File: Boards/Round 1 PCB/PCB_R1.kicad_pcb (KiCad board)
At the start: 2 copper layers, 98.4 x 93.1 mm, 67 parts, among them J1 Screw_Terminal_01x12, J10 Screw_Terminal_01x03, J11 Screw_Terminal_01x12, J12 Screw_Terminal_01x03, J13 Screw_Terminal_01x03, J14 Screw_Terminal_01x03, J15 Screw_Terminal_01x03, J16 Screw_Terminal_01x03, J17 Screw_Terminal_01x03, J18 Screw_Terminal_01x03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

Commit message: PCB Design contraints
Updated and tested width and clearene constraints and everything was ok, one unconnected thing. Footprints not updated
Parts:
- C14, C15: value C -> 180uF
- C17: value C -> 2.2uF
- C8, C9: value C -> 20nF
- D3: value SP0503BAHT -> SP0503BAHTG
- L1: value L -> 60uH
- L2: value L -> 2.2uH
- R1, R3: value R_UVLO -> 40K
- R2: value R_UVLO_2 -> 20k
- R4: value R_UVLO_2 -> 20K
- R5: value R_FB_1 -> 2.8K
- R6, R8: value R_FB_2 -> 1K
- R7: value R_FB_1 -> 1.5K
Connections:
- net /V_in renamed +7.5V
- U1 pad 13: /3.3V_OUT -> +3.3V

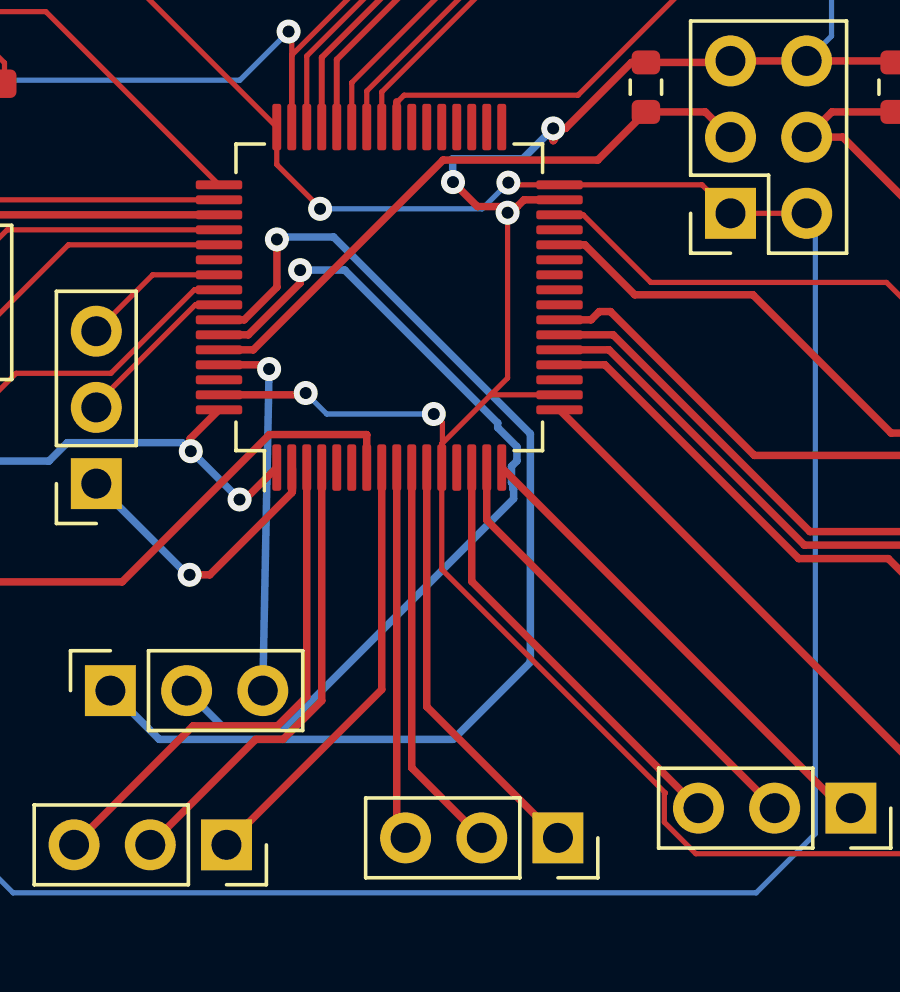
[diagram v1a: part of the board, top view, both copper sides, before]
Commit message: fixed PCB contraints and re-routed something that broke
yea, that
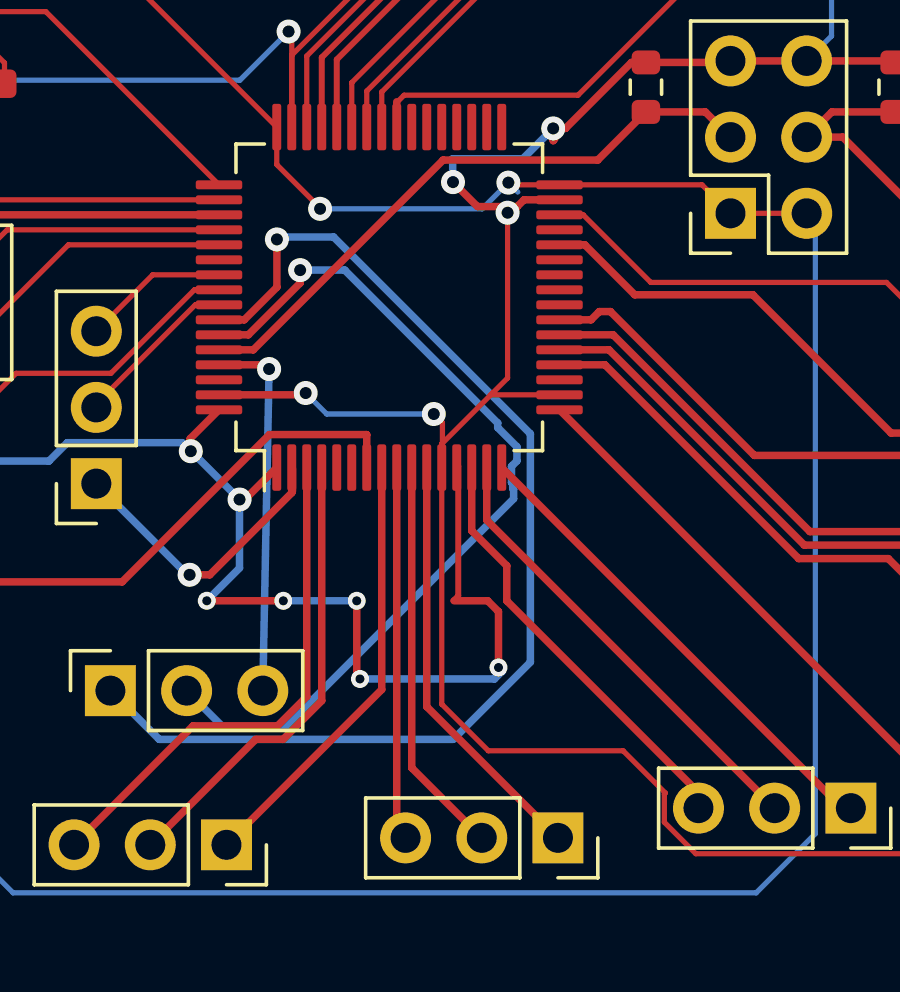
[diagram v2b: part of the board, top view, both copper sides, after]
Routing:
- net +3.3V: track 269.5 -> 294.6 mm, vias 8 -> 13
- net GND: track 612.0 -> 614.6 mm

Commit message: R1 - no builder errors
woot woot
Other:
- board size 98.4 x 93.1 mm -> 97 x 89.5 mm
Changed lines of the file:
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@@
     )
   )
-  (gr_rect (start 50.292 30.099) (end 148.717 123.19)
+  (gr_rect (start 52 31) (end 149 120.5)
     (stroke (width 0.1) (type default)) (fill none) (layer "Edge.Cuts"))
   (dimension (type aligned) (layer "F.Cu")
-    (pts (xy 50.165 30.48) (xy 148.59 30.099))
+    (pts (xy 50.165 30.48) (xy 150 30))
     (height -6.240529)
-    (gr_text "98.4257 mm" (at 99.346375 22.249031 0.2217890065) (layer "F.Cu")
+    (gr_text "99.8362 mm" (at 100.043842 22.199564 0.2754721516) (layer "F.Cu")
       (effects (font (size 1.5 1.5) (thickness 0.3)))
     )
@@
   )
   (dimension (type aligned) (layer "F.Cu")
-    (pts (xy 150.622 30.353) (xy 150.749 123.317))
-    (height -15.259748)
-    (gr_text "92.9641 mm" (at 167.745232 76.811694 270.0782729) (layer "F.Cu")
+    (pts (xy 150.5 28) (xy 150.749 123.317))
+    (height -15.751651)
+    (gr_text "95.3173 mm" (at 168.176091 75.61265 270.1496755) (layer "F.Cu")
       (effects (font (size 1.5 1.5) (thickness 0.3)))
     )
@@
     (polygon
       (pts
-        (xy 50.165 30.48)
-        (xy 148.59 30.099)
-        (xy 148.717 123.063)
-        (xy 50.164999 123.444)
+        (xy 50.665 28.48)
+        (xy 150.5 28)
+        (xy 150 123.063)
+        (xy 50.164999 122.5)
         (xy 50.292 36.703)
       )
@@
     (polygon
       (pts
-        (xy 50.165 30.48)
-        (xy 148.59 30.226)
-        (xy 148.717 122.809)
-        (xy 50.419 123.19)
-        (xy 50.419 29.972)
+        (xy 50.665 28.5)
+        (xy 149.5 28.5)
+        (xy 150 122.809)
+        (xy 50.419 122.5)
+        (xy 50.5 29.972)
       )
     )

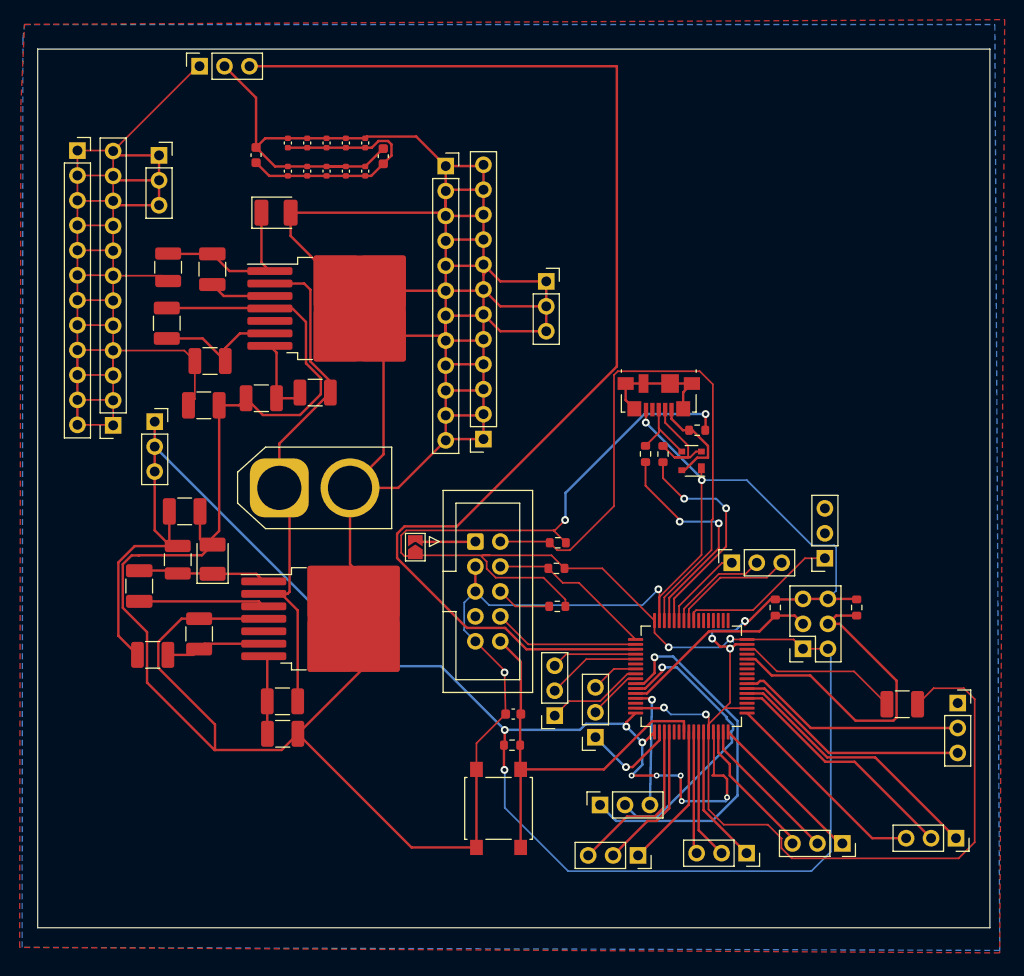
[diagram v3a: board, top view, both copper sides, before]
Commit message: r1 SMD footprint updates
changed component footprints on the board and schematic to use free smd components
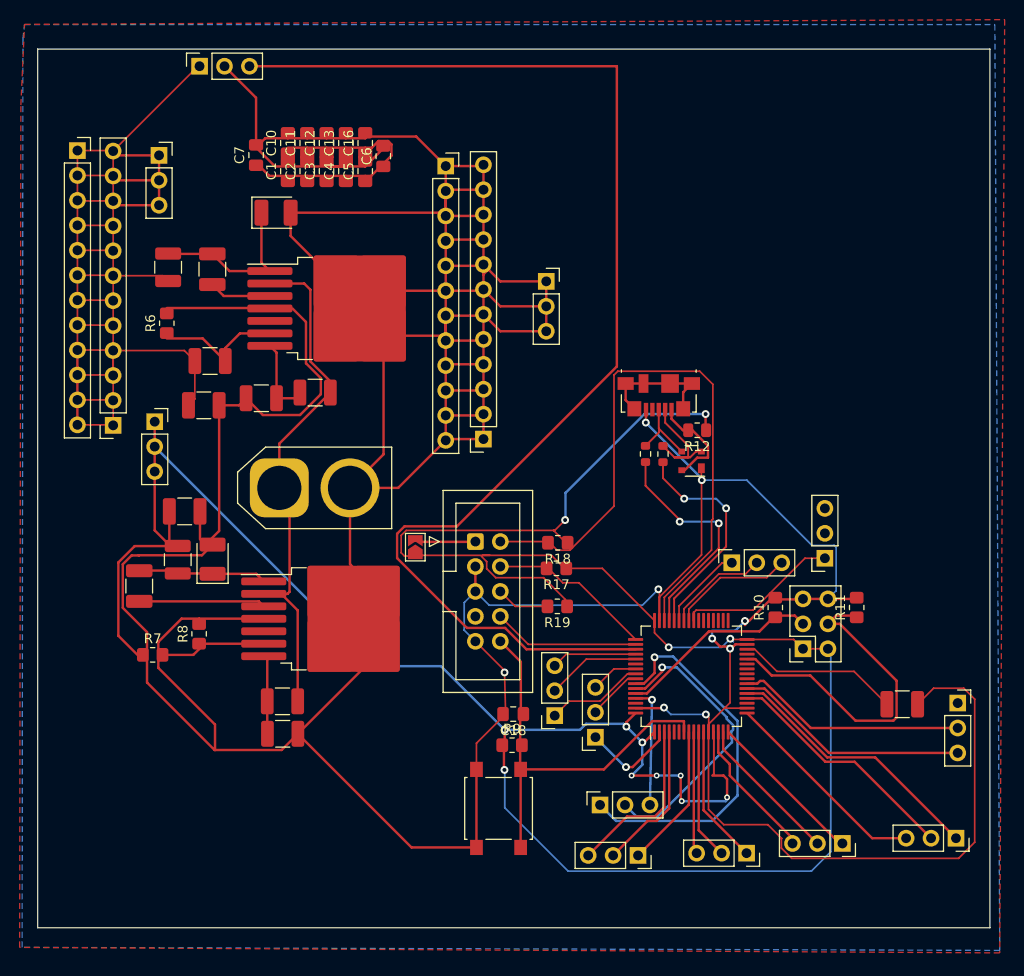
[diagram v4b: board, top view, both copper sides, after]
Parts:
- C1, C10, C11, C12, C13, C16, C2, C3, C4, C5: footprint Capacitor_SMD:C_0402_1005Metric -> Capacitor_SMD:C_0805_2012Metric_Pad1.18x1.45mm_HandSolder
- C18, C6, C7: footprint Capacitor_SMD:C_0603_1608Metric -> Capacitor_SMD:C_0805_2012Metric_Pad1.18x1.45mm_HandSolder
- R10, R11, R17, R18, R19, R9: footprint Resistor_SMD:R_0603_1608Metric -> Resistor_SMD:R_0805_2012Metric_Pad1.20x1.40mm_HandSolder
- R12: footprint Resistor_SMD:R_0603_1608Metric -> Resistor_SMD:R_0805_2012Metric
- R6, R7, R8: footprint Resistor_SMD:R_1210_3225Metric_Pad1.30x2.65mm_HandSolder -> Resistor_SMD:R_0805_2012Metric_Pad1.20x1.40mm_HandSolder

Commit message: Resistor 0805 update
all resistors and capacitors are 0805 now, thanks Dad
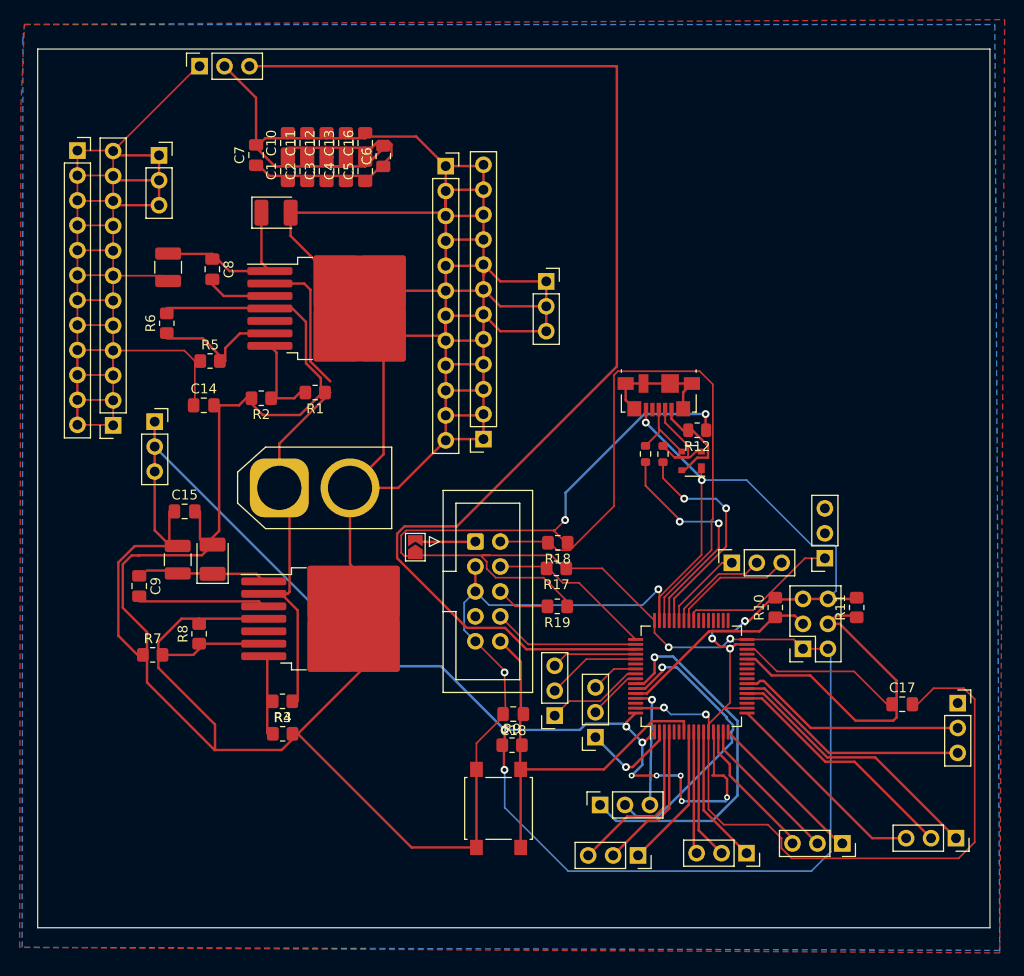
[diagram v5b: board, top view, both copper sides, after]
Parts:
- C14, C15, C17, C8, C9: footprint Capacitor_SMD:C_1210_3225Metric_Pad1.33x2.70mm_HandSolder -> Capacitor_SMD:C_0805_2012Metric_Pad1.18x1.45mm_HandSolder
- R1, R2, R3, R4, R5: footprint Resistor_SMD:R_1210_3225Metric_Pad1.30x2.65mm_HandSolder -> Resistor_SMD:R_0805_2012Metric_Pad1.20x1.40mm_HandSolder
